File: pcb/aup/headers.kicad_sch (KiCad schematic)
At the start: 6 parts, among them J1 QSH-060-01-L-D-A, J2 QSH-060-01-L-D-A, J3 QTH-060-01-L-D-A, J4 QTH-060-01-L-D-A, J5 QSH-030-01-L-D-A, J6 QTH-030-01-L-D-A

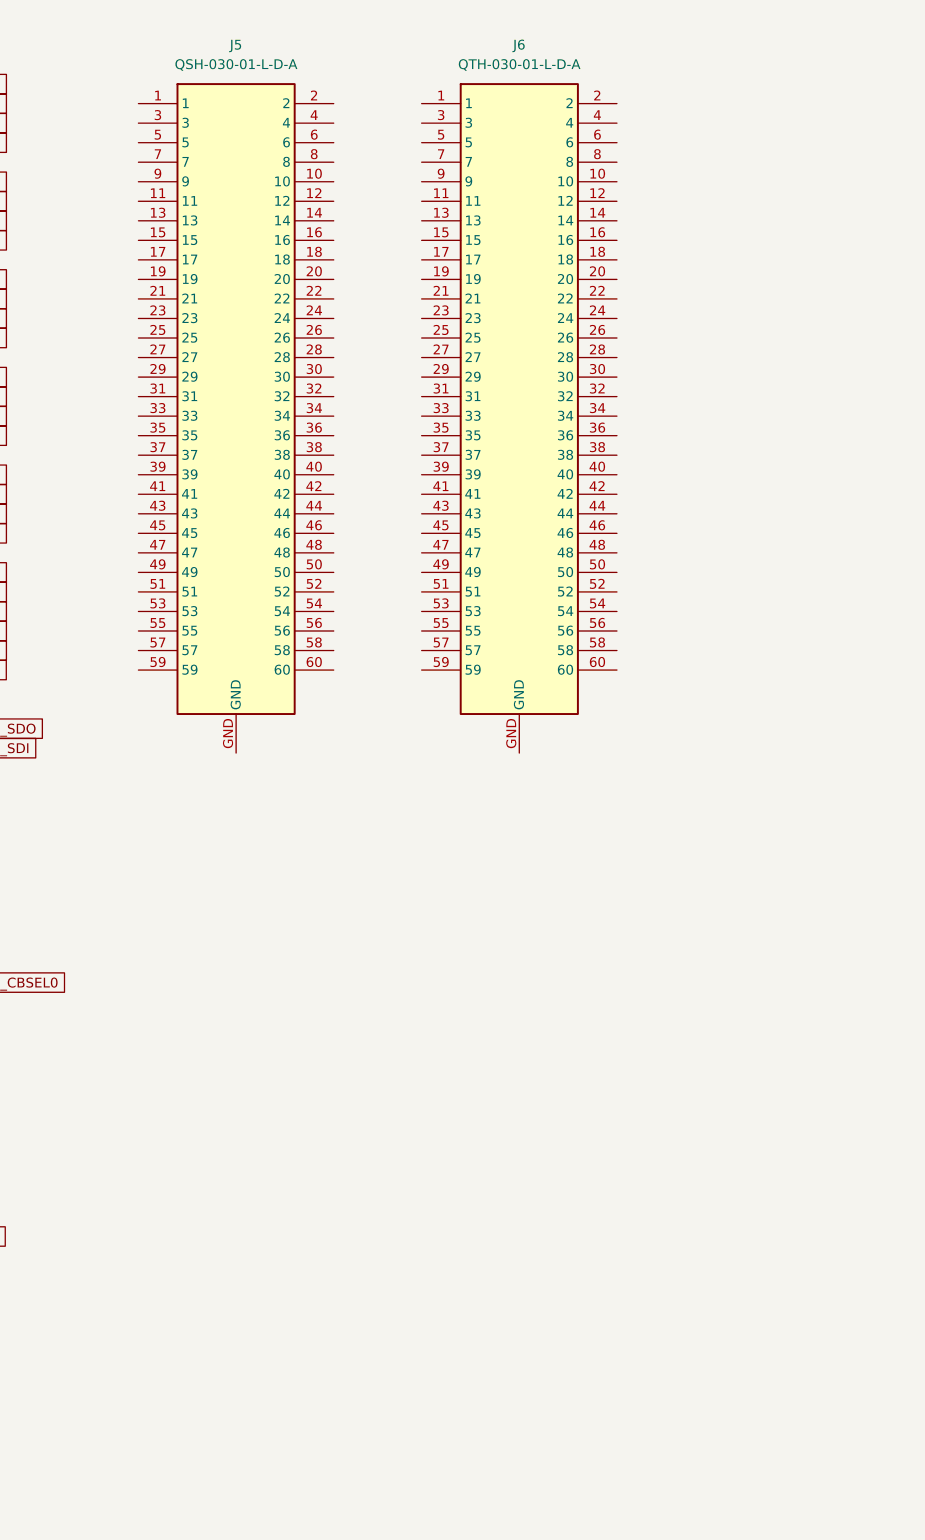
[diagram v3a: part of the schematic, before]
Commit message: Start working out GTP diff pair routing
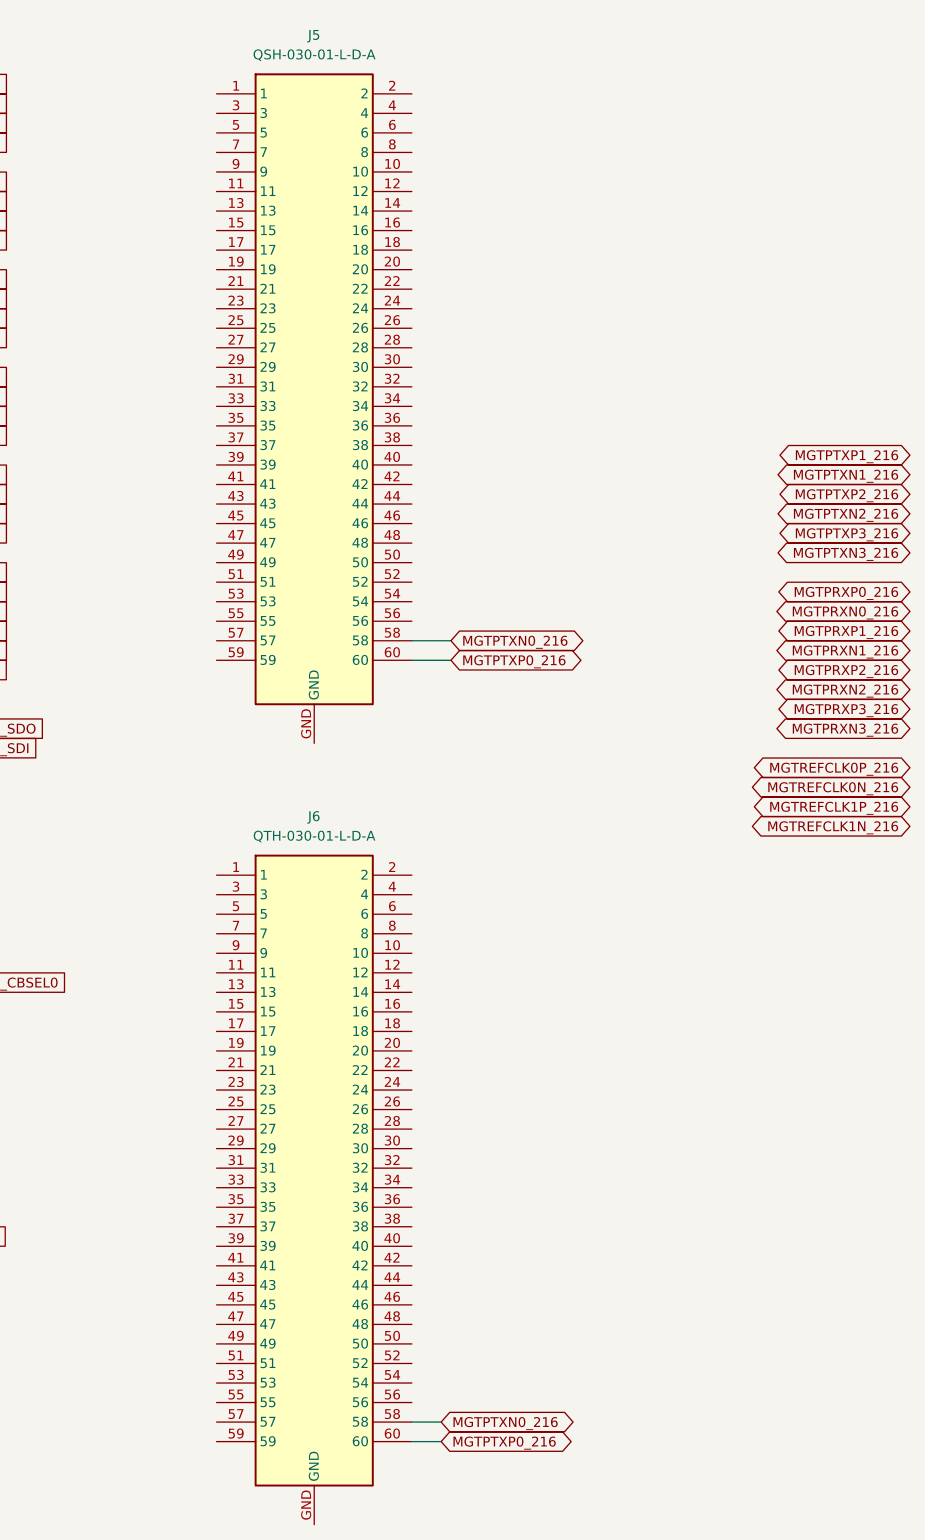
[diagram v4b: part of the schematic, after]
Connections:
- net MGTPTXN0_216: now reaches J6.58
- net MGTPTXN0_216: now also J5.58
- net MGTPTXP0_216: now reaches J6.60
- net MGTPTXP0_216: now also J5.60
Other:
- moved on the sheet: J5, J6

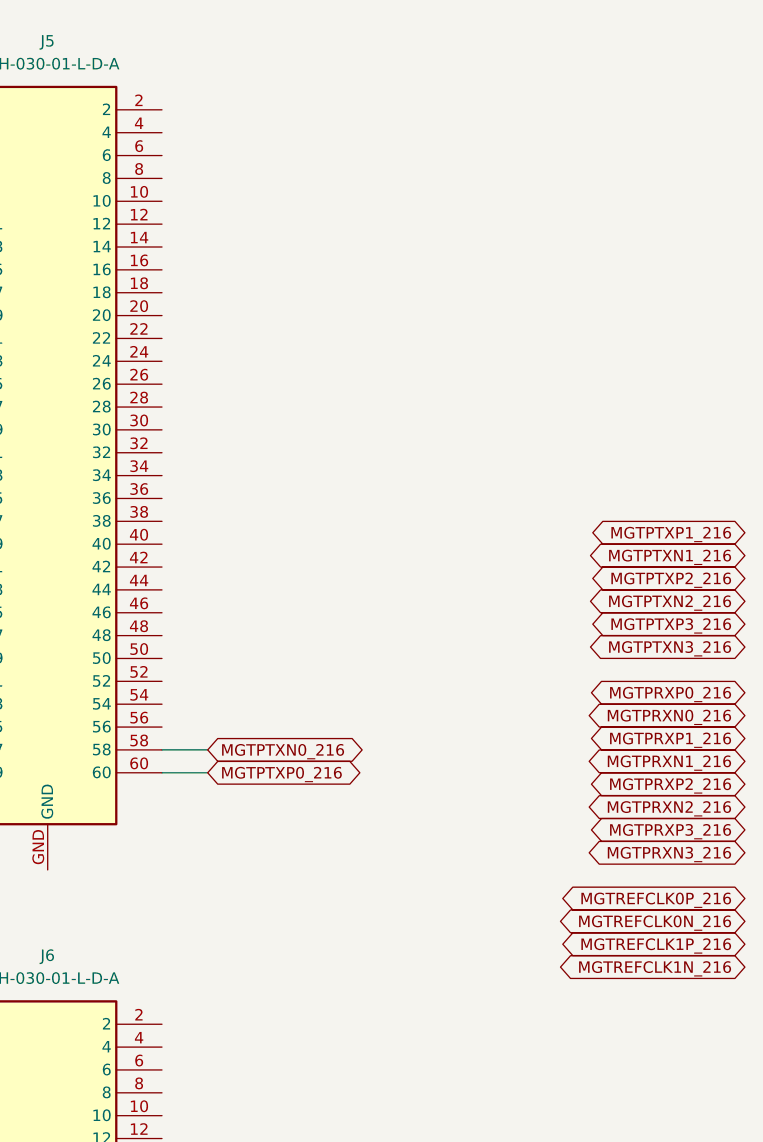
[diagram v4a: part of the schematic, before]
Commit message: GTP diff pairs routed, but not tuned
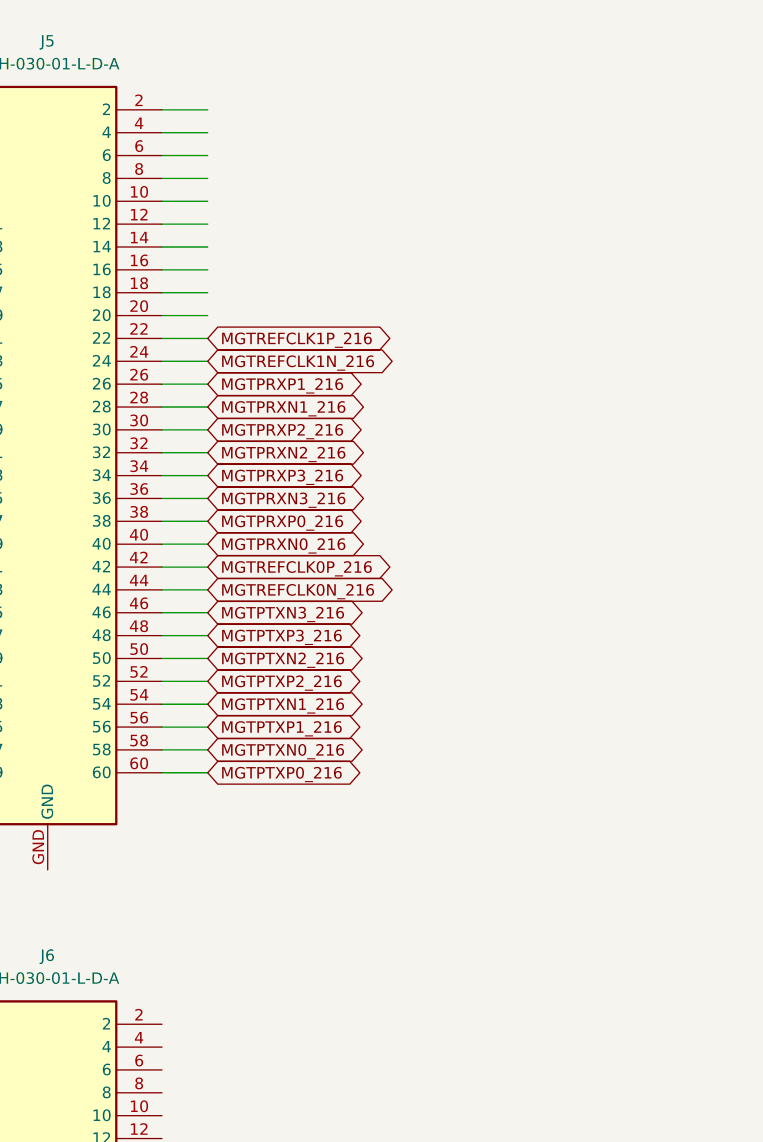
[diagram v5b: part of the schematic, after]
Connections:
- net MGTPRXN0_216: now also J5.40
- net MGTPRXN1_216: now also J5.28
- net MGTPRXN2_216: now also J5.32
- net MGTPRXN3_216: now also J5.36
- net MGTPRXP0_216: now also J5.38
- net MGTPRXP1_216: now also J5.26
- net MGTPRXP2_216: now also J5.30
- net MGTPRXP3_216: now also J5.34
- net MGTPTXN1_216: now also J5.54
- net MGTPTXN2_216: now also J5.50
- net MGTPTXN3_216: now also J5.46
- net MGTPTXP1_216: now also J5.56
- net MGTPTXP2_216: now also J5.52
- net MGTPTXP3_216: now also J5.48
- net MGTREFCLK0N_216: now also J5.44
- net MGTREFCLK0P_216: now also J5.42
- net MGTREFCLK1N_216: now also J5.24
- net MGTREFCLK1P_216: now also J5.22
